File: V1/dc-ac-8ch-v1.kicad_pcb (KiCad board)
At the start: 2 copper layers, 98 x 67.8 mm, 101 parts, among them J1 DB142V-5.08-8P, J2 DB142V-5.08-2P, J3 DB142V-5.08-8P, J4 DB142V-5.08-2P, U1 MOC3063S, U2 MOC3063S, U3 MOC3063S, U4 MOC3063S, U5 MOC3063S, U6 MOC3063S, U7 MOC3063S, U8 MOC3063S

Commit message: Under development
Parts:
- removed J3: DB142V-5.08-8P, Tales:TerminalBlock_Dibo_DB142V-5.08-8P_1x08_P5.08mm_Vertical
- moved R10 0.07 mm to (74.0, 96.5)
- moved R13 0.07 mm to (95.0, 96.5)
- moved R14 0.07 mm to (89.0, 96.5)
- moved R15 0.07 mm to (86.0, 96.5)
- moved R18 0.07 mm to (107.0, 96.5)
- moved R19 0.07 mm to (101.0, 96.5)
- moved R20 0.07 mm to (98.0, 96.5)
- moved R23 0.07 mm to (119.0, 96.5)
- moved R24 0.07 mm to (113.0, 96.5)
- moved R25 0.07 mm to (110.0, 96.5)
- moved R28 0.07 mm to (131.0, 96.5)
- moved R29 0.07 mm to (125.0, 96.5)
- moved R3 0.07 mm to (71.0, 96.5)
- moved R30 0.07 mm to (122.0, 96.5)
- moved R33 0.07 mm to (143.0, 96.5)
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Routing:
- net NEUTRAL: track 0.00 -> 157.6 mm, vias 0 -> 16
- net GND: track 0.00 -> 76.5 mm, vias 0 -> 16
- net Net-(J1-Pin_8): track 0.00 -> 41.3 mm
- net Net-(J1-Pin_1): track 0.00 -> 36.9 mm
- net Net-(J1-Pin_7): track 0.00 -> 34.4 mm
- net Net-(J1-Pin_2): track 0.00 -> 29.9 mm
- net Net-(J1-Pin_6): track 0.00 -> 27.5 mm
- net Net-(J1-Pin_3): track 0.00 -> 23.0 mm
- net Net-(J1-Pin_5): track 0.00 -> 20.7 mm
- net Net-(J1-Pin_4): track 0.00 -> 18.9 mm
- net Net-(D9-G): track 0.00 -> 15.1 mm, vias 0 -> 2
- net Net-(D6-G): track 0.00 -> 15.1 mm, vias 0 -> 2
- net Net-(D15-G): track 0.00 -> 15.1 mm, vias 0 -> 2
- net Net-(D12-G): track 0.00 -> 15.1 mm, vias 0 -> 2
- net Net-(D3-G): track 0.00 -> 15.1 mm, vias 0 -> 2
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- added copper zone on B.Cu, net GND

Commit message: Development
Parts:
- removed the REF** at (74.0, 69.0)
- added J2: DB142V-5.08-4P, Tales:TerminalBlock_Dibo_DB142V-5.08-4P_1x04_P5.08mm_Vertical_copy, F.Cu at (167.0, 125.5)
- added J4: DB142V-5.08-4P, Tales:TerminalBlock_Dibo_DB142V-5.08-4P_1x04_P5.08mm_Vertical_copy, F.Cu at (130.0, 66.5)
- added J5: DB142V-5.08-4P, Tales:TerminalBlock_Dibo_DB142V-5.08-4P_1x04_P5.08mm_Vertical_copy, F.Cu at (178.0, 66.5)
- added REF**: Logo_Tramontina_25mm_Silk, Tales:Logo_Tramontina_25mm_Silk, F.Cu at (113.5, 117.0)
- J1: value DB142V-5.08-8P -> DB142V-5.08-4P; footprint Tales:TerminalBlock_Dibo_DB142V-5.08-8P_1x08_P5.08mm_Vertical -> Tales:TerminalBlock_Dibo_DB142V-5.08-4P_1x04_P5.08mm_Vertical_copy
- moved D12 40.1 mm to (142.8, 86.7)
- moved D15 40.1 mm to (154.8, 86.7)
- moved D18 40.1 mm to (166.8, 86.7)
- moved D9 40.1 mm to (130.8, 86.7)
- moved C1 40.1 mm to (105.0, 110.0)
- moved C10 40.1 mm to (156.0, 93.5)
- moved C11 40.1 mm to (165.0, 110.0)
- moved C12 40.1 mm to (168.0, 93.5)
- moved C13 40.1 mm to (177.0, 110.0)
- moved C14 40.1 mm to (180.0, 93.5)
- moved C15 40.1 mm to (189.0, 110.0)
- moved C16 40.1 mm to (192.0, 93.5)
- moved C2 40.1 mm to (108.0, 93.5)
- moved C3 40.1 mm to (117.0, 110.0)
- moved C4 40.1 mm to (120.0, 93.5)
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- renumbered J2 to J3, J4 to J6
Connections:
- R21 pad 1: Net-(J1-Pin_5) -> Net-(J2-Pin_1)
- R22 pad 2: Net-(J1-Pin_5) -> Net-(J2-Pin_1)
- R26 pad 1: Net-(J1-Pin_6) -> Net-(J2-Pin_2)
- R27 pad 2: Net-(J1-Pin_6) -> Net-(J2-Pin_2)
- R31 pad 1: Net-(J1-Pin_7) -> Net-(J2-Pin_3)
- R32 pad 2: Net-(J1-Pin_7) -> Net-(J2-Pin_3)
- R36 pad 1: Net-(J1-Pin_8) -> Net-(J2-Pin_4)
- R37 pad 2: Net-(J1-Pin_8) -> Net-(J2-Pin_4)
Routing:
- net GND: track 76.5 -> 229.4 mm, vias 16 -> 17
- net NEUTRAL: track 157.6 -> 274.9 mm
- net Net-(J1-Pin_8): track 41.3 -> 0.00 mm
- net Net-(J1-Pin_7): track 34.4 -> 0.00 mm
- net Net-(J1-Pin_6): track 27.5 -> 0.00 mm
- net Net-(J2-Pin_4): track 0.00 -> 25.5 mm
- net Net-(J2-Pin_1): track 0.00 -> 24.1 mm
- net Net-(D3-A2): track 12.4 -> 33.6 mm
- net Net-(D15-A2): track 12.4 -> 33.6 mm
- net Net-(J1-Pin_5): track 20.7 -> 0.00 mm
- net Net-(D24-A2): track 12.4 -> 32.9 mm
- net Net-(D12-A2): track 12.4 -> 32.9 mm
- net Net-(J2-Pin_3): track 0.00 -> 18.8 mm
- net Net-(J2-Pin_2): track 0.00 -> 18.5 mm
- net Net-(D6-A2): track 12.4 -> 28.5 mm
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- added copper zone on B.Cu, net NEUTRAL
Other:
- board text added: "0V"
- board text added: "E1"
- board text added: "E2"
- board text added: "E3"
- board text added: "E4"
- board text added: "E5"
- board text added: "E6"
- board text added: "E7"
- board text added: "E8"
- board text added: "N"
- board text added: "S1"
- board text added: "S2"
- board text added: "S3"
- board text added: "S4"
- board text added: "S5"
- board text added: "S6"
- board text added: "S7"
- board text added: "S8"
- board text added: "SUPORTES PCI METALTEX SP7 1x pé macho 9 mm 1x pé fêmea 9 mm 2x espaçadores 30 mm 1x espaçador 20 mm Comprimento total 98 mm Largura da placa 67,8 mm"
- board text removed: "SUPORTES PCI METALTEX SP7 1x pé macho 9 mm 1x pé fêmea 9 mm 2x espaçadores 45 mm Comprimento total 108 mm Largura da placa 67,8 mm"

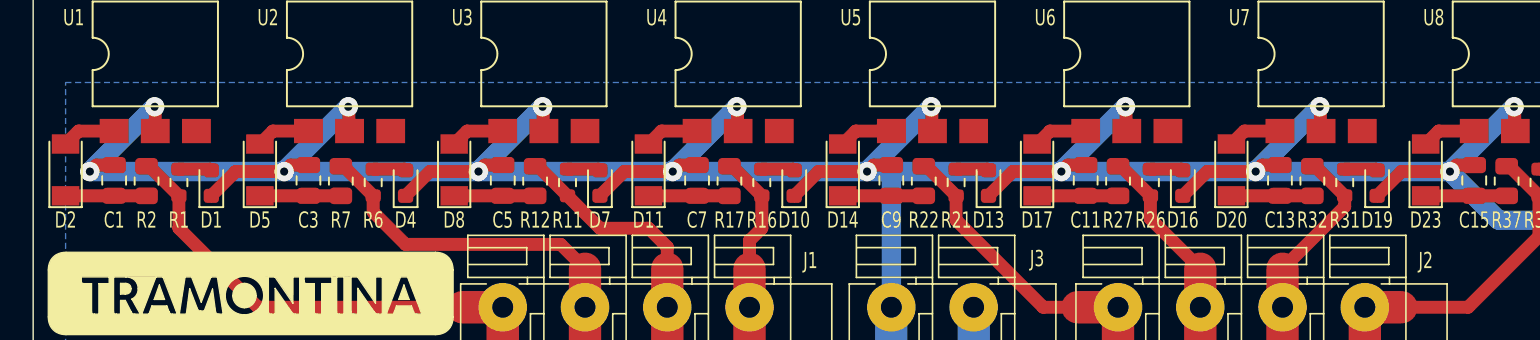
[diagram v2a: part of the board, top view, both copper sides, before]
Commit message: Zener diode replaced
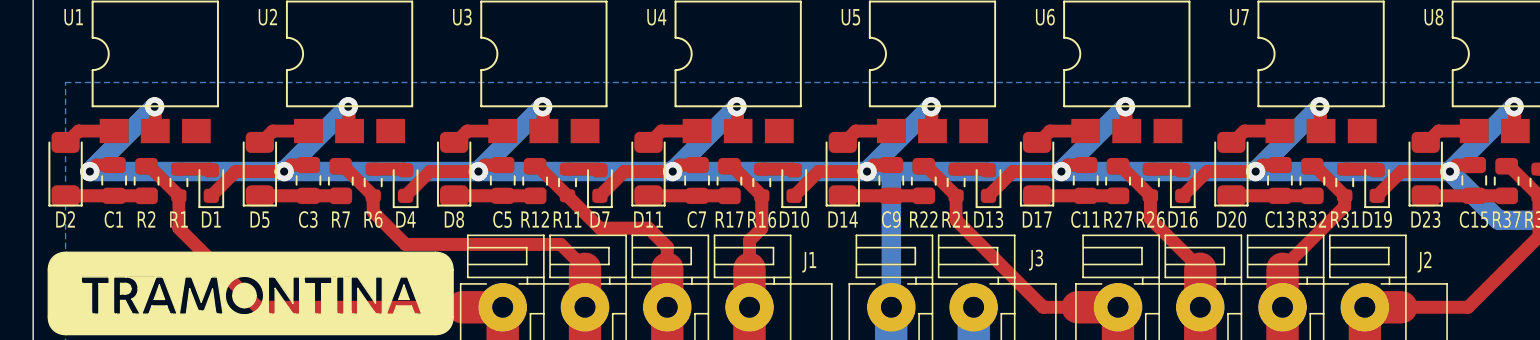
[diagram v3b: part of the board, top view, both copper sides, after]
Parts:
- D11, D14, D17, D2, D20, D23, D5, D8: footprint Tales:D_MiniMELF -> Tales:D_SOD-123
- moved D11 0.05 mm to (138.0, 109.3)
- moved D14 0.05 mm to (150.0, 109.3)
- moved D17 0.05 mm to (162.0, 109.3)
- moved D2 0.05 mm to (102.0, 109.3)
- moved D20 0.05 mm to (174.0, 109.3)
- moved D23 0.05 mm to (186.0, 109.3)
- moved D5 0.05 mm to (114.0, 109.3)
- moved D8 0.05 mm to (126.0, 109.3)

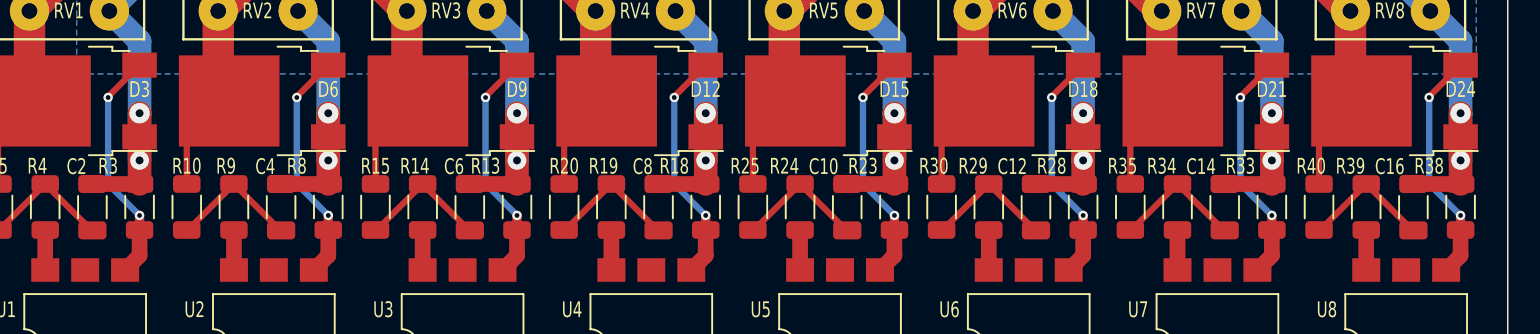
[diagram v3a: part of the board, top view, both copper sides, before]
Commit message: Replace resistor for basic part
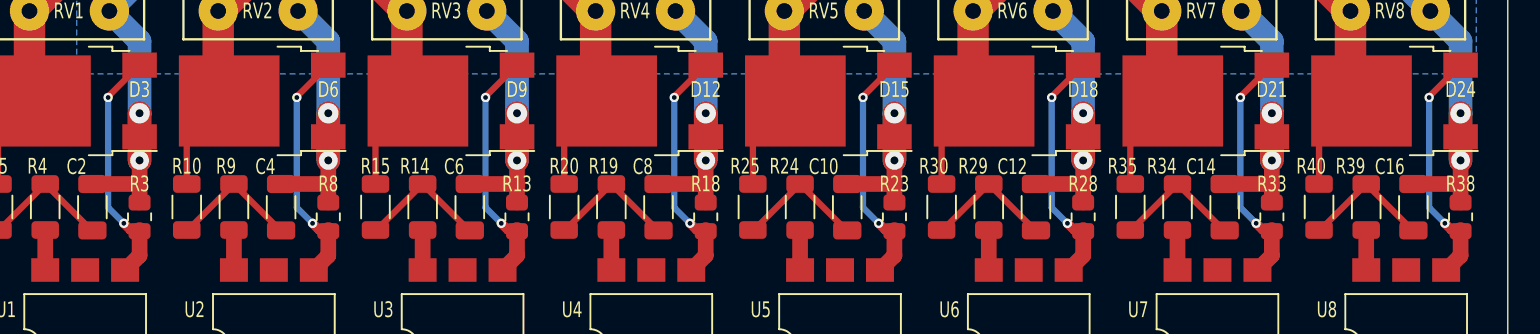
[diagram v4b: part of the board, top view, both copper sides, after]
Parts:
- R13, R18, R23, R28, R3, R33, R38, R8: value 390R/250mW -> 390R/125mW; footprint Tales:R_1206_3216Metric -> Tales:R_0805_2012Metric
- moved R13 0.62 mm to (135.0, 94.1)
- moved R18 0.62 mm to (147.0, 94.1)
- moved R23 0.62 mm to (159.0, 94.1)
- moved R28 0.62 mm to (171.0, 94.1)
- moved R3 0.62 mm to (111.0, 94.1)
- moved R33 0.62 mm to (183.0, 94.1)
- moved R38 0.62 mm to (195.0, 94.1)
- moved R8 0.62 mm to (123.0, 94.1)
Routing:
- net NEUTRAL: track 274.9 -> 284.3 mm
